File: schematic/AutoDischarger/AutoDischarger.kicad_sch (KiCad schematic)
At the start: 0 parts

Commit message: Initial schematic
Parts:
- added C1: 1 uF, symbol Device:C
- added C2: 10 uF, symbol Device:C
- added C3: 100 nF, symbol Device:C
- added D1: LED, symbol Device:LED
- added IC1: AP7375-50SA-7, Package_TO_SOT_SMD:SOT-23, symbol SamacSys_Parts:MCP1703AT-5002E_CB
- added IC2: PIC18F15Q40-I_SS, SOP65P780X200-20N, symbol SamacSys_Parts:PIC18F15Q40-I_SS
- added J1: ICSP, symbol Connector_Generic:Conn_01x05
- added J2: Balance Lead, symbol Connector_Generic:Conn_01x07
- added R1: 1K, symbol Device:R
- added S1: PTS647SK38SMTR2LFS, PTS647SK38SMTR2LFS, symbol SamacSys_Parts:PTS647SK38SMTR2LFS
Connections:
- new net: IC2.19 (RA0/ICSPDAT), J1.4 (Pin_4)
- new net: IC2.18 (RA1/ICSPCLK), J1.5 (Pin_5)
- new net: D1.2 (A), R1.1
- new net: IC2.9 (RC7), R1.2
- new net: IC2.8 (RC6), S1.1 (NO_1), S1.2 (NO_2)
- new net +5V: C2.1, C3.1, IC1.2 (VOUT), IC2.1 (VDD), J1.2 (Pin_2)
- new net +8V: C1.1, IC1.1 (VIN), J2.3 (Pin_3)
- new net Discharge Control/C1: IC2.16 (RC0)
- new net Discharge Control/C2: IC2.15 (RC1)
- new net Discharge Control/C3: IC2.14 (RC2)
- new net Discharge Control/C4: IC2.7 (RC3)
- new net Discharge Control/C5: IC2.6 (RC4)
- new net Discharge Control/C6: IC2.5 (RC5)
- new net Discharge Control/VC1: IC2.2 (RA5), J2.2 (Pin_2)
- new net Discharge Control/VC3: J2.4 (Pin_4)
- new net Discharge Control/VC4: J2.5 (Pin_5)
- new net Discharge Control/VC5: J2.6 (Pin_6)
- new net Discharge Control/VC6: J2.7 (Pin_7)
- new net GND: C1.2, C2.2, C3.2, D1.1 (K), IC1.3 (GND), IC2.20 (VSS), J1.3 (Pin_3), J2.1 (Pin_1), S1.3 (COM_1), S1.4 (COM_2)
- new net VPP: IC2.4 (~{MCLR}/VPP/RA3), J1.1 (Pin_1)
- new net Voltage Sense/SHDN: IC2.17 (RA2)
- new net Voltage Sense/V_SENSE2: IC2.3 (RA4)
- new net Voltage Sense/V_SENSE3: IC2.10 (RB7)
- new net Voltage Sense/V_SENSE4: IC2.11 (RB6)
- new net Voltage Sense/V_SENSE5: IC2.12 (RB5)
- new net Voltage Sense/V_SENSE6: IC2.13 (RB4)
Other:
- added sheet Discharge Control (discharge_control.kicad_sch)
- added sheet Voltage Sense (v_sense.kicad_sch.kicad_sch)

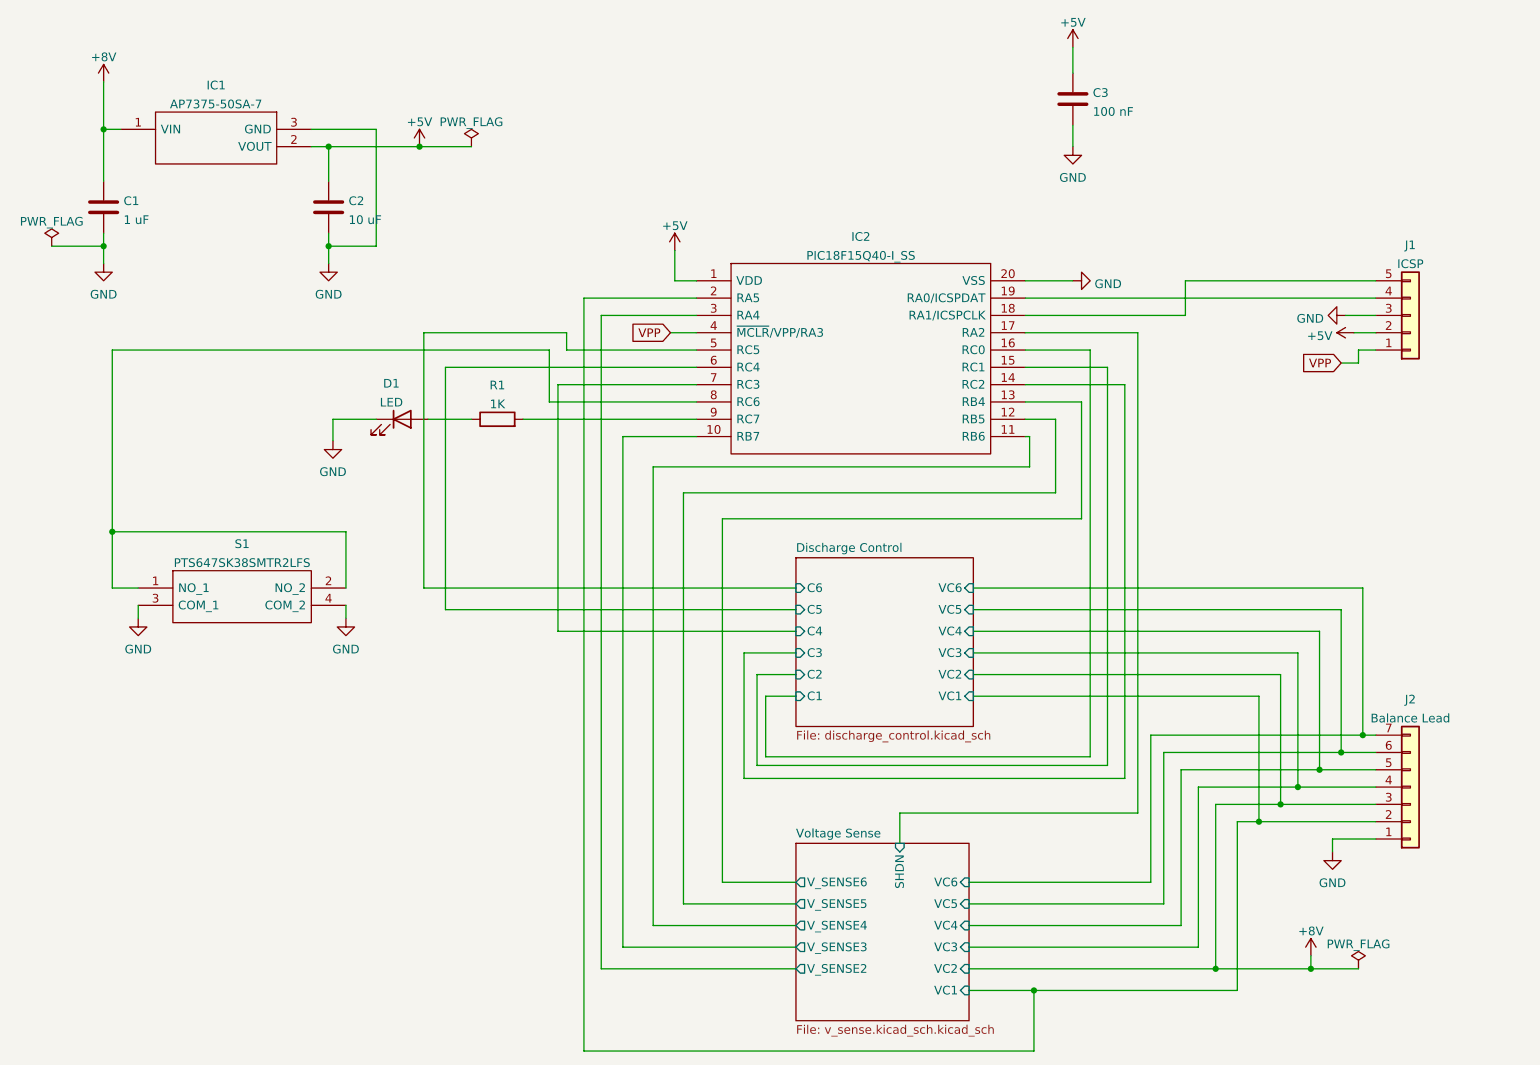
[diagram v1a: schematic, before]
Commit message: Some schematic fixes and assigned footprints.
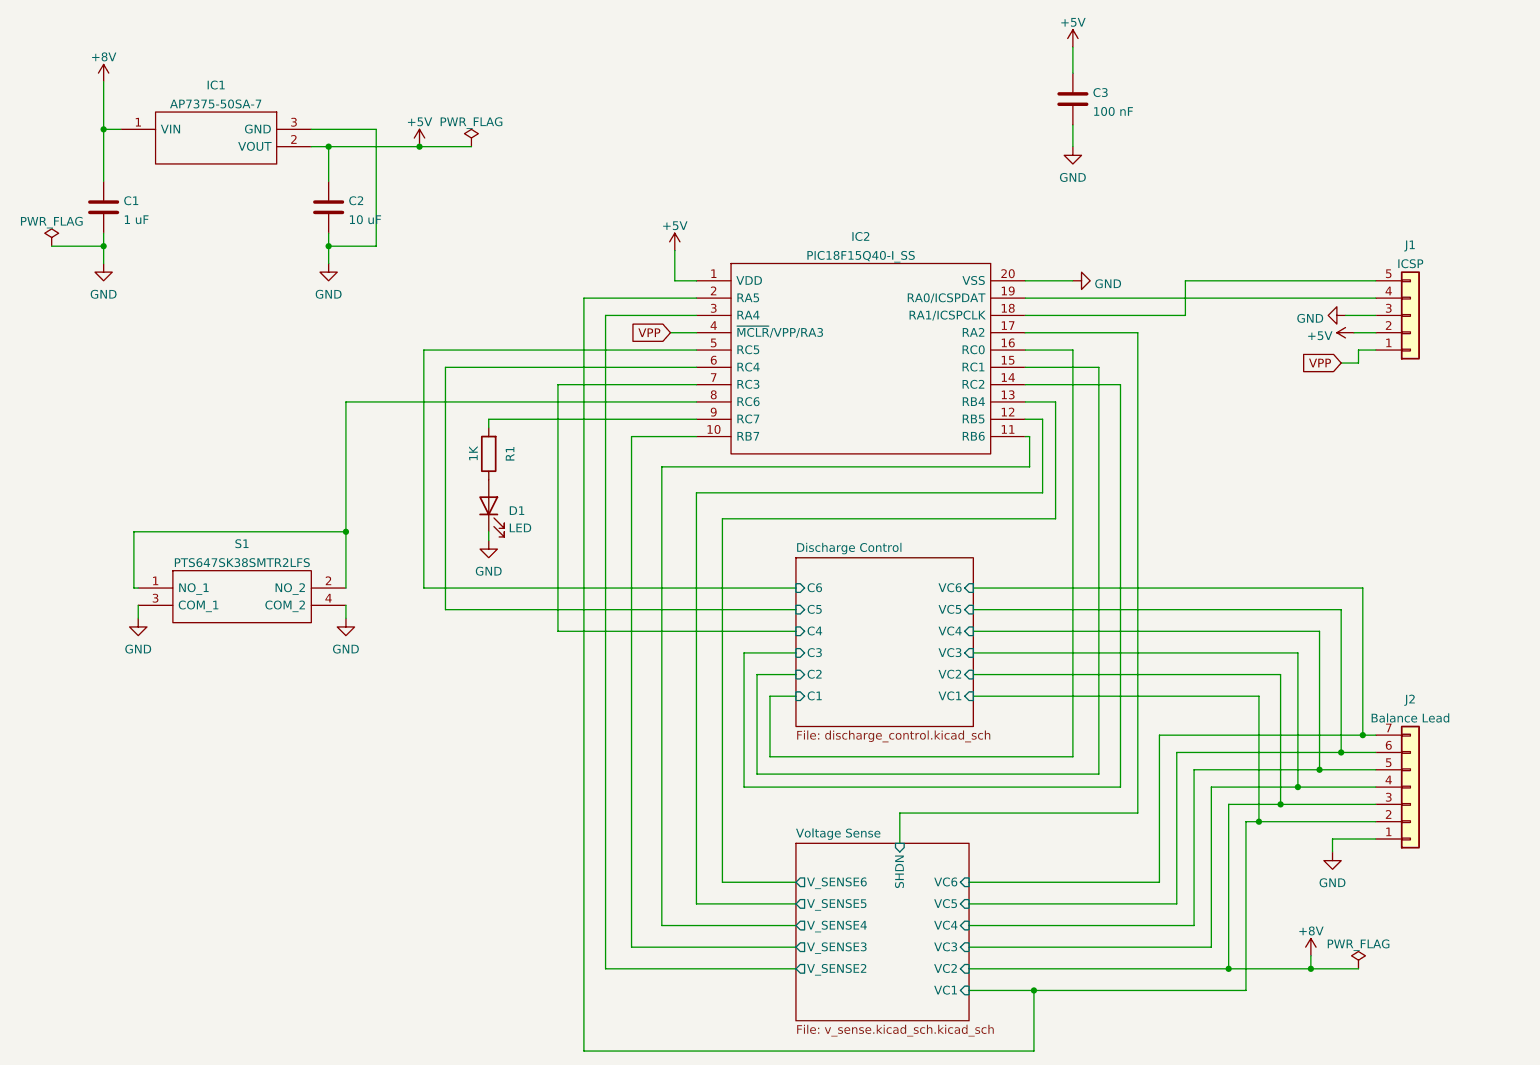
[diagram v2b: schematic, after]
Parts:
- C1, C2, C3: footprint (none) -> Capacitor_SMD:C_0603_1608Metric
- D1: footprint (none) -> LED_SMD:LED_0603_1608Metric
- IC2: footprint SOP65P780X200-20N -> SamacSys_Parts:SOP65P780X200-20N
- J1: footprint (none) -> Connector_PinHeader_2.54mm:PinHeader_1x05_P2.54mm_Vertical
- J2: footprint (none) -> Connector_JST:JST_XH_B7B-XH-A_1x07_P2.50mm_Vertical
- R1: footprint (none) -> Resistor_SMD:R_0603_1608Metric
- S1: footprint PTS647SK38SMTR2LFS -> SamacSys_Parts:PTS647SK38SMTR2LFS
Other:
- company: Quantum Embedded System -> Quantum Embedded Systems
- moved on the sheet: D1, R1

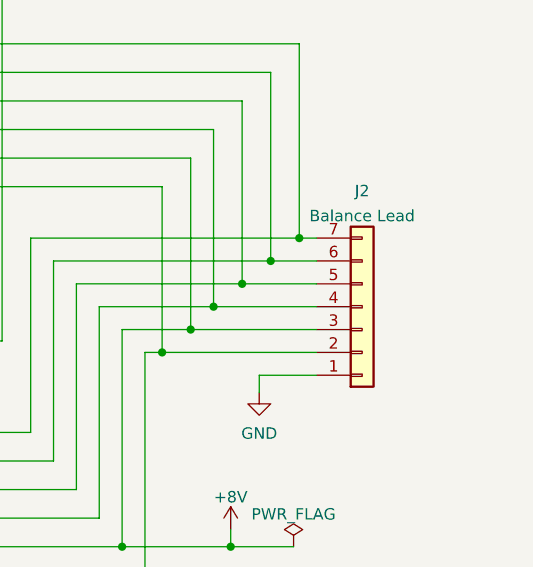
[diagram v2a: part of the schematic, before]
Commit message: Some schematic and footprint fixes
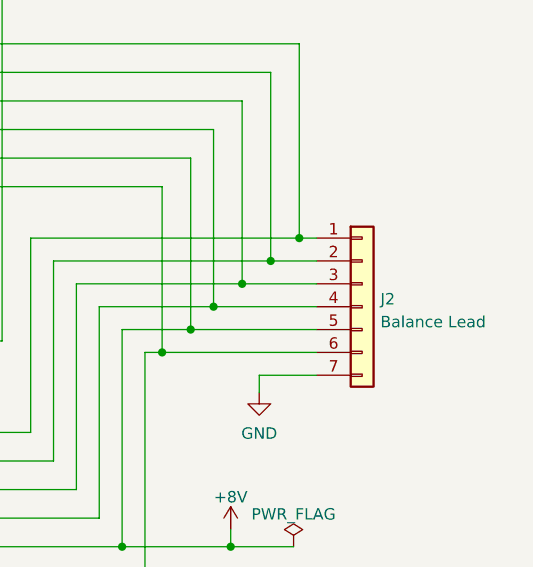
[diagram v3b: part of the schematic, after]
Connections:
- net +8V: now also J2.5 (Pin_5); no longer J2.3 (Pin_3)
- net Discharge Control/VC1: now also J2.6 (Pin_6); no longer J2.2 (Pin_2)
- net Discharge Control/VC4: now also J2.3 (Pin_3); no longer J2.5 (Pin_5)
- net Discharge Control/VC5: now also J2.2 (Pin_2); no longer J2.6 (Pin_6)
- net Discharge Control/VC6: now also J2.1 (Pin_1); no longer J2.7 (Pin_7)
- net GND: now also J2.7 (Pin_7); no longer J2.1 (Pin_1)
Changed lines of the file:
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@@
     (pin "1")
   )
-  (symbol (lib_id "Connector_Generic:Conn_01x07") (at 216.535 130.175 0) (mirror x) (unit 1)
-    (in_bom yes) (on_board yes) (fields_autoplaced)
-    (property "Reference" "J2" (id 0) (at 216.535 117.3185 0))
-    (property "Value" "Balance Lead" (id 1) (at 216.535 120.0936 0))
+  (symbol (lib_id "Connector_Generic:Conn_01x07") (at 216.535 130.175 0) (unit 1)
+    (in_bom yes) (on_board yes) (fields_autoplaced)
+    (property "Reference" "J2" (id 0) (at 218.567 129.3403 0)
+      (effects (font (size 1.27 1.27)) (justify left))
+    )
+    (property "Value" "Balance Lead" (id 1) (at 218.567 131.8772 0)
+      (effects (font (size 1.27 1.27)) (justify left))
+    )
     (property "Footprint" "Connector_JST:JST_XH_B7B-XH-A_1x07_P2.50mm_Vertical" (id 2) (at 216.535 130.175 0)
       (effects (font (size 1.27 1.27)) hide)
@@
     )
     (path "/77bcabc8-1188-4d31-8dd6-5a41ab350454/b3179e89-cad8-48ce-93ab-34954f0b69ac"
-      (reference "Q1") (unit 1) (value "2N7002_HAMR") (footprint "SamacSys_Parts:2N7002HAMR")
+      (reference "Q1") (unit 1) (value "2N7002_HAMR") (footprint "Package_TO_SOT_SMD:SOT-23")
     )
     (path "/77bcabc8-1188-4d31-8dd6-5a41ab350454/68325520-3143-4288-bd7a-829a3b59b5b1"
-      (reference "Q2") (unit 1) (value "2N7002_HAMR") (footprint "SamacSys_Parts:2N7002HAMR")
+      (reference "Q2") (unit 1) (value "2N7002_HAMR") (footprint "Package_TO_SOT_SMD:SOT-23")
     )
     (path "/77bcabc8-1188-4d31-8dd6-5a41ab350454/73b19b83-770c-4207-9dc3-0552baffc670"
-      (reference "Q3") (unit 1) (value "2N7002_HAMR") (footprint "SamacSys_Parts:2N7002HAMR")
+      (reference "Q3") (unit 1) (value "2N7002_HAMR") (footprint "Package_TO_SOT_SMD:SOT-23")
     )
     (path "/77bcabc8-1188-4d31-8dd6-5a41ab350454/ff6ac747-707b-4961-a102-563a11d935be"
-      (reference "Q4") (unit 1) (value "2N7002_HAMR") (footprint "SamacSys_Parts:2N7002HAMR")
+      (reference "Q4") (unit 1) (value "2N7002_HAMR") (footprint "Package_TO_SOT_SMD:SOT-23")
     )
     (path "/77bcabc8-1188-4d31-8dd6-5a41ab350454/208ec227-77c9-4feb-b025-6f61c0e27115"
-      (reference "Q5") (unit 1) (value "2N7002_HAMR") (footprint "SamacSys_Parts:2N7002HAMR")
+      (reference "Q5") (unit 1) (value "2N7002_HAMR") (footprint "Package_TO_SOT_SMD:SOT-23")
     )
     (path "/77bcabc8-1188-4d31-8dd6-5a41ab350454/5440c0b5-3780-40bc-a032-9b590edf50b4"
-      (reference "Q6") (unit 1) (value "2N7002_HAMR") (footprint "SamacSys_Parts:2N7002HAMR")
+      (reference "Q6") (unit 1) (value "2N7002_HAMR") (footprint "Package_TO_SOT_SMD:SOT-23")
     )
     (path "/77bcabc8-1188-4d31-8dd6-5a41ab350454/2d779771-b1ab-4fac-bd33-f70aa0cd8f0f"
-      (reference "Q7") (unit 1) (value "2N7002_HAMR") (footprint "SamacSys_Parts:2N7002HAMR")
+      (reference "Q7") (unit 1) (value "2N7002_HAMR") (footprint "Package_TO_SOT_SMD:SOT-23")
     )
     (path "/77bcabc8-1188-4d31-8dd6-5a41ab350454/472d0607-7da0-4976-b990-1a464a56da15"
-      (reference "Q8") (unit 1) (value "2N7002_HAMR") (footprint "SamacSys_Parts:2N7002HAMR")
+      (reference "Q8") (unit 1) (value "2N7002_HAMR") (footprint "Package_TO_SOT_SMD:SOT-23")
     )
     (path "/77bcabc8-1188-4d31-8dd6-5a41ab350454/dc895304-8464-4d89-85fc-c6a56738014e"
-      (reference "Q9") (unit 1) (value "2N7002_HAMR") (footprint "SamacSys_Parts:2N7002HAMR")
+      (reference "Q9") (unit 1) (value "2N7002_HAMR") (footprint "Package_TO_SOT_SMD:SOT-23")
     )
     (path "/77bcabc8-1188-4d31-8dd6-5a41ab350454/f39af658-5429-4804-a5c1-003f749136ca"
-      (reference "Q10") (unit 1) (value "2N7002_HAMR") (footprint "SamacSys_Parts:2N7002HAMR")
+      (reference "Q10") (unit 1) (value "2N7002_HAMR") (footprint "Package_TO_SOT_SMD:SOT-23")
     )
     (path "/77bcabc8-1188-4d31-8dd6-5a41ab350454/451eac64-965a-410c-b4e9-0f8cb31c7d32"
-      (reference "Q11") (unit 1) (value "2N7002_HAMR") (footprint "SamacSys_Parts:2N7002HAMR")
+      (reference "Q11") (unit 1) (value "2N7002_HAMR") (footprint "Package_TO_SOT_SMD:SOT-23")
     )
     (path "/15eb6ae6-6d8f-499f-a0b3-7ad0e61d54f9"
